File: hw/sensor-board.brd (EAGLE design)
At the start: 50 x 40 mm, 17 parts, among them U1 LT1762EMS8-3.3PBF, U2 ULN2003LVPWR, U3 ULN2003LVPWR, U4 PCA9685PW, U5 AT42QT1110-AU, X1 MOLEX-501331-1007, X2 MOLEX-501953-0407, X3 MOLEX-501953-0407, X4 MOLEX-501953-0407

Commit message: Update LED driver package for easier hand soldering.
New land patterns for PCA9685PW and ULN2003LV hae 0.5 mm of pads
extending past the IC pins to allow the soldering iron to make contact
with the pad.
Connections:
- new net VDD: U4.28
- net VDD_5: no longer U4.28
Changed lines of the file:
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@@
 </signal>
 <signal name="VDD_5">
-<contactref element="U4" pad="28"/>
 <contactref element="U1" pad="5"/>
 <contactref element="U1" pad="8"/>
@@
 </signal>
 <signal name="GND">
-<contactref element="U4" pad="14"/>
 <contactref element="U5" pad="5"/>
 <contactref element="U5" pad="21"/>
@@
 <contactref element="U2" pad="8"/>
 <contactref element="U3" pad="8"/>
+<contactref element="U4" pad="14"/>
 <wire x1="25.95" y1="33.1" x2="34.55" y2="33.9" width="0" layer="19" extent="1-1"/>
 <wire x1="16.3" y1="32.525" x2="25.95" y2="33.1" width="0" layer="19" extent="1-1"/>
 <wire x1="5.775" y1="11" x2="16.3" y2="32.525" width="0" layer="19" extent="1-1"/>
 <wire x1="5.775" y1="9" x2="5.775" y2="11" width="0" layer="19" extent="1-1"/>
-<wire x1="17.025" y1="2.45" x2="5.775" y2="9" width="0" layer="19" extent="1-1"/>
-<wire x1="22.6625" y1="1.775" x2="17.025" y2="2.45" width="0" layer="19" extent="1-1"/>
-<wire x1="37.775" y1="2.2" x2="22.6625" y2="1.775" width="0" layer="19" extent="1-1"/>
+<wire x1="17.025" y1="2.3" x2="5.775" y2="9" width="0" layer="19" extent="1-1"/>
+<wire x1="22.4625" y1="1.775" x2="17.025" y2="2.3" width="0" layer="19" extent="1-1"/>
+<wire x1="37.775" y1="2.05" x2="22.4625" y2="1.775" width="0" layer="19" extent="1-1"/>
 <wire x1="-5.875" y1="-14.75" x2="5.775" y2="9" width="0" layer="19" extent="1-1"/>
 <wire x1="-5.875" y1="-19" x2="-5.875" y2="-14.75" width="0" layer="19" extent="1-1"/>
@@
 <wire x1="5.775" y1="3" x2="31.45" y2="29.2" width="0" layer="19" extent="1-1"/>
 </signal>
+<signal name="VDD">
+<contactref element="U4" pad="28"/>
+</signal>
 </signals>

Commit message: Connect capsense controller/buttons/B2B connector.
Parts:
- added C10, C11, C12, C5, C6, C7, C8, C9: 0.015uF 16V, rcl:C0402K
- added R1, R2, R3, R4, R5, R6, R7, R8: 4.7k, myrcl:R0402
- added TP1, TP2, TP3, TP4: PTR1TP06R, testpad:TP06R
- C2, C3, C4: device rcl:C0603K -> rcl:C0402K
- moved X4 41.2 mm to (45.5, 31.2)
- moved X3 40.2 mm to (5.50, 31.2)
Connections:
- net N$6 renamed VDD_3_3
- new net N$10: C8.1, U5.8
- new net N$11: C9.1, U5.10
- new net N$12: C10.1, U5.12
- new net N$13: C11.1, U5.20
- new net N$14: C12.1, U5.23
- new net N$15: C5.2, R1.1, U5.1
- new net N$16: C6.2, R2.1, U5.3
- new net N$17: C7.2, R3.1, U5.6
- new net N$18: C8.2, R4.1, U5.9
- new net N$19: C9.2, R5.1, U5.11
- new net N$20: C10.2, R6.1, U5.13
- new net N$21: C11.2, R7.1, U5.19
- new net N$22: C12.2, R8.1, U5.22
- new net N$23: R5.2, X4.1
- new net N$24: R6.2, X4.2
- new net N$25: R7.2, X4.3
- new net N$26: R8.2, X4.4
- new net N$27: R4.2, TP4.TP, X3.4
- new net N$28: R3.2, TP3.TP, X3.3
- new net N$29: R2.2, TP2.TP, X3.2
- new net N$30: R1.2, TP1.TP, X3.1
- new net N$6: C5.1, U5.32
- new net N$7: C6.1, U5.2
- new net N$9: C7.1, U5.7

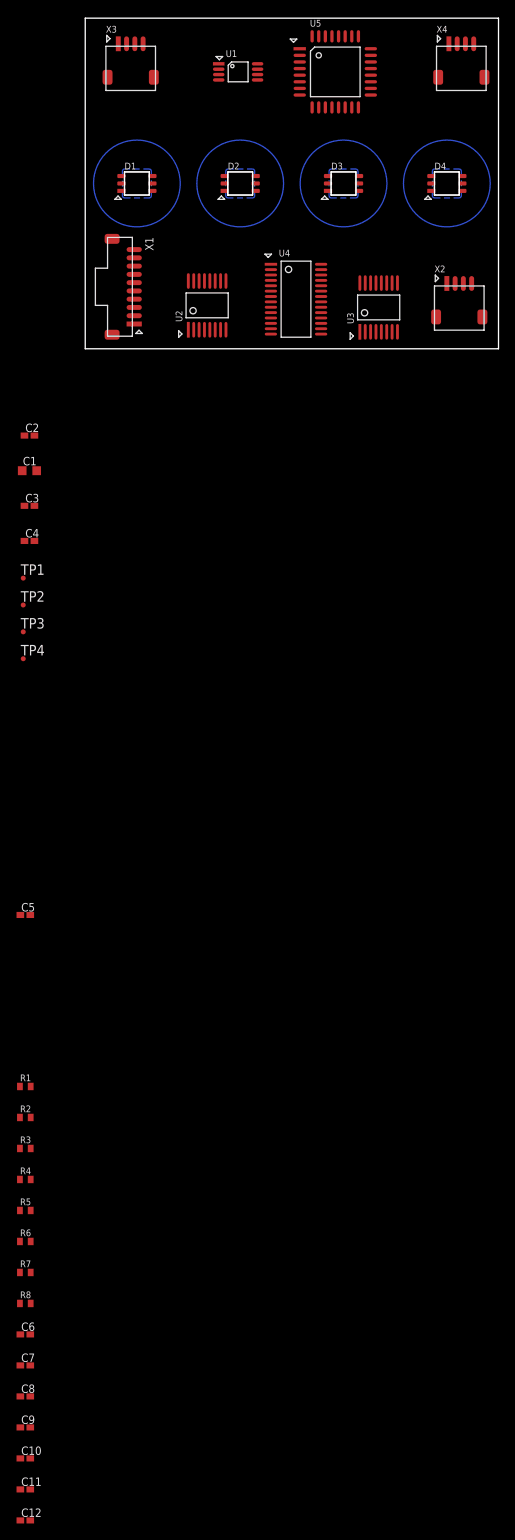
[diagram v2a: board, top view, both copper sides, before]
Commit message: Partly complete layout.
Pending schematic tasks:
1.  Replace 10 pin sensor board to main board connector with a higher
    pin count variant for unrouted signals on LED controller and
    RST,CHANGE pins on touch controller.
2.  Add pull ups on control and comm lines of touch and led ICs,
    as needed.
3.  Add mecahnism to set I2C address on LED controller.
4.  Identify purpose of and route COM pin on ULN2003LV.

Pending layout tasks:
1.  Route power and ground to top half and bottom right parts of board.
2.  Consider rotating touch IC 90 degrees counter clockwise to better
    match positions of b2b sensor connector and capsense buttons.
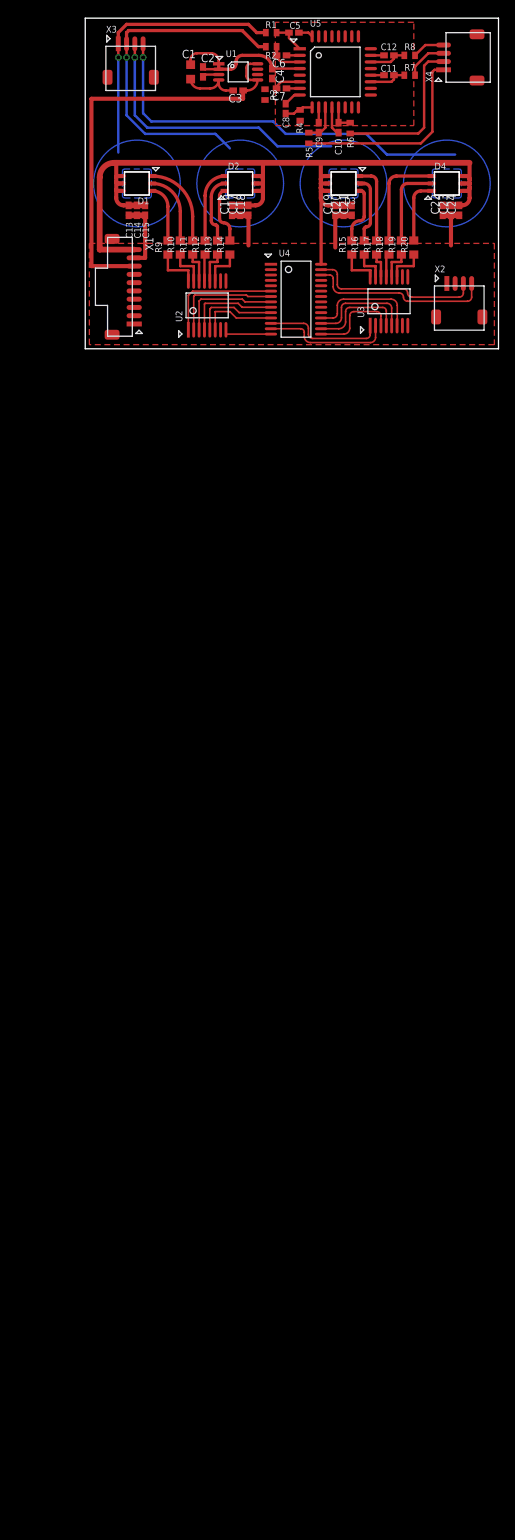
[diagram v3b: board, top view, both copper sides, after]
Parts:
- removed TP1, TP2, TP3, TP4: PTR1TP06R, testpad:TP06R
- added C13, C14, C15, C16, C17, C18, C19, C20, C21, C22, C23, C24: 0.01uF 16V, rcl:C0402K
- added R10, R11, R12, R13, R14, R15, R16, R17, R18, R19, R20, R9: 60R 145mW, myrcl:R0603
- moved C12 182.6 mm to (36.8, 35.5)
- moved C11 176.7 mm to (36.8, 33.1)
- moved C10 165.4 mm to (30.6, 26.8), turned to 90 degrees
- moved C9 161.2 mm to (28.2, 26.8), turned to 270 degrees
- moved C8 159.0 mm to (24.2, 29.1), turned to 270 degrees
- moved R8 158.0 mm to (39.2, 35.5)
- moved C6 157.8 mm to (23.8, 35.5), turned to 180 degrees
- moved C7 157.6 mm to (23.8, 31.5), turned to 180 degrees
- moved R7 152.1 mm to (39.2, 33.1)
- moved R6 140.3 mm to (32.0, 26.7), turned to 270 degrees
- moved R5 134.2 mm to (27.1, 25.5), turned to 270 degrees
- moved R4 133.0 mm to (26.0, 28.2), turned to 270 degrees
- moved R2 132.9 mm to (22.5, 36.5), turned to 180 degrees
- moved R1 130.9 mm to (22.5, 38.2), turned to 180 degrees
- moved R3 130.8 mm to (21.8, 30.8), turned to 270 degrees
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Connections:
- removed net N$27: R4.2, TP4.TP, X3.4
- removed net N$28: R3.2, TP3.TP, X3.3
- removed net N$29: R2.2, TP2.TP, X3.2
- removed net N$30: R1.2, TP1.TP, X3.1
- removed net VDD: U4.28
- new net KEY1: R1.2, X3.1
- new net KEY2: R2.2, X3.2
- new net KEY3: R3.2, X3.3
- new net KEY4: R4.2, X3.4
- new net LEDOUT_A1: U2.1, U4.6
- new net LEDOUT_A2: U2.2, U4.7
- new net LEDOUT_A3: U2.3, U4.8
- new net LEDOUT_A4: U2.4, U4.9
- new net LEDOUT_A5: U2.5, U4.10
- new net LEDOUT_A6: U2.6, U4.11
- new net LEDOUT_B1: U3.1, U4.12
- new net LEDOUT_B2: U3.2, U4.13
- new net LEDOUT_B3: U3.3, U4.15
- new net LEDOUT_B4: U3.4, U4.16
- new net LEDOUT_B5: U3.5, U4.17
- new net LEDOUT_B6: U3.6, U4.18
- new net N$31: D4.1, R20.2
- new net N$32: D1.1, R11.2
- new net N$33: D1.2, R10.2
- new net N$34: D3.3, R15.2
- new net N$35: D2.3, R12.2
- new net N$36: D2.2, R13.2
- new net N$37: R15.1, U3.16
- new net N$38: R16.1, U3.15
- new net N$39: D3.1, R17.2
- new net N$40: D3.2, R16.2
- new net N$41: D4.3, R18.2
- new net N$42: D4.2, R19.2
- new net N$55: R17.1, U3.14
- new net N$56: R18.1, U3.13
- new net N$57: R19.1, U3.12
- new net N$58: R20.1, U3.11
- new net N$59: D2.1, R14.2
- new net N$60: D1.3, R9.2
- new net N$61: R9.1, U2.16
- new net N$62: R10.1, U2.15
- new net N$63: R11.1, U2.14
- new net N$64: R12.1, U2.13
- new net N$65: R13.1, U2.12
- new net N$66: R14.1, U2.11
- new net SCL: U4.26, X2.4
- new net SDA: U4.27, X2.3
- net GND: now also C13.1, C14.1, C15.1, C16.1, C17.1, C18.1, C19.1, C20.1, C21.1, C22.1, C23.1, C24.1, X2.2
- net VDD_5: now also C13.2, C14.2, C15.2, C16.2, C17.2, C18.2, C19.2, C20.2, C21.2, C22.2, C23.2, C24.2, D1.4, D1.5, D1.6, D2.4, D2.5, D2.6, D3.4, D3.5, D3.6, D4.4, D4.5, D4.6, U4.28, X1.1, X2.1
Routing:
- net VDD_5: track 0.00 -> 162.6 mm
- net KEY4: track 0.00 -> 48.2 mm, vias 0 -> 1
- net KEY2: track 0.00 -> 41.9 mm, vias 0 -> 1
- net GND: track 0.00 -> 40.5 mm
- net KEY3: track 0.00 -> 34.0 mm, vias 0 -> 1
- net KEY1: track 0.00 -> 33.2 mm, vias 0 -> 1
- net N$23: track 0.00 -> 24.2 mm
- net SCL: track 0.00 -> 22.0 mm
- net SDA: track 0.00 -> 20.7 mm
- net VDD_3_3: track 0.00 -> 19.7 mm
- net N$24: track 0.00 -> 19.3 mm
- net LEDOUT_B2: track 0.00 -> 15.3 mm
- net LEDOUT_B1: track 0.00 -> 14.5 mm
- net LEDOUT_A1: track 0.00 -> 14.4 mm
- net LEDOUT_A2: track 0.00 -> 13.5 mm
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- added copper zone on layer 1, net GND
- added copper zone on layer 16, net KEY1
- added copper zone on layer 16, net KEY2
- added copper zone on layer 16, net KEY3
- added copper zone on layer 16, net KEY4
- removed copper zone on layer 16, net N$1

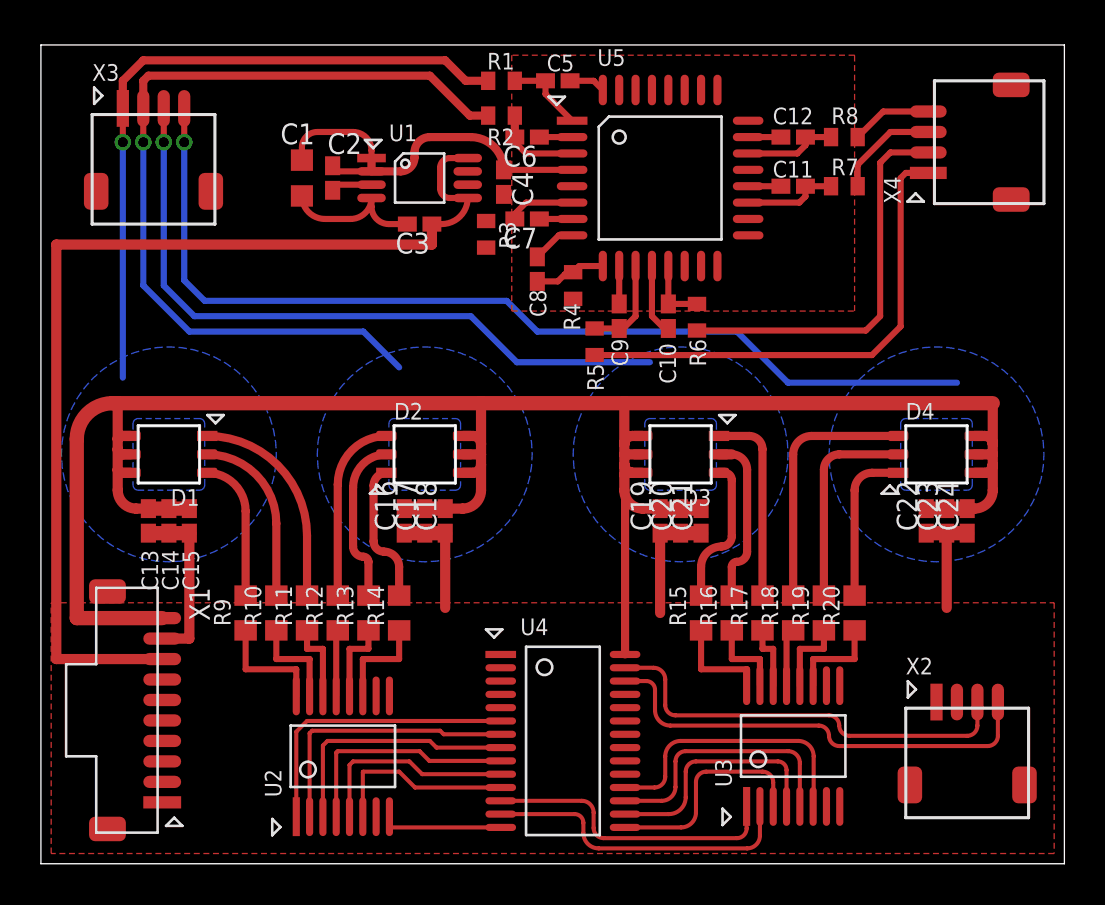
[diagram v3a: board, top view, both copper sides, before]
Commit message: Compact the layout of LED driving circuitry.
Additional space has been created for a larger sensor to main board
connector.
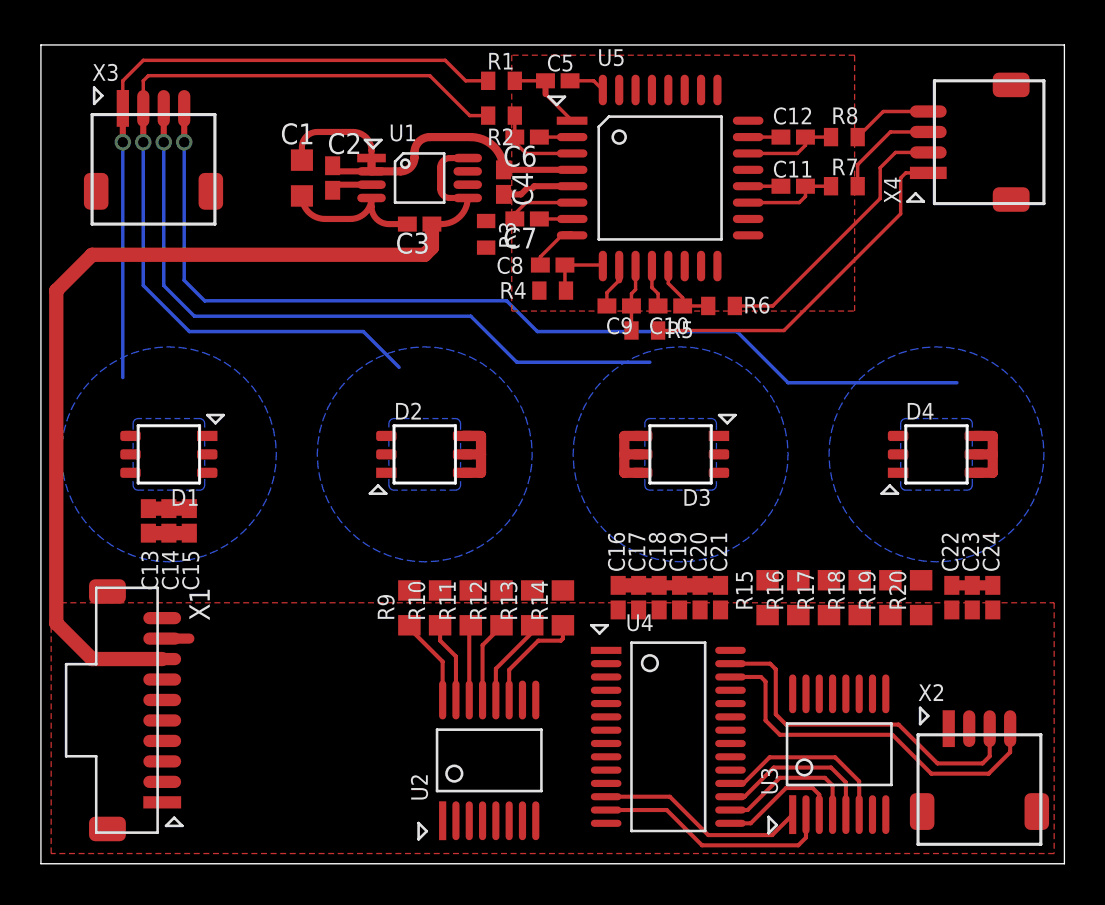
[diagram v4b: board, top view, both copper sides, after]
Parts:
- moved C16 11.1 mm to (28.2, 13.0)
- moved C17 11.1 mm to (29.2, 13.0)
- moved C18 11.1 mm to (30.2, 13.0)
- moved R10 8.00 mm to (19.5, 12.5)
- moved R11 8.00 mm to (21.0, 12.5)
- moved R12 8.00 mm to (22.5, 12.5)
- moved R13 8.00 mm to (24.0, 12.5)
- moved R14 8.00 mm to (25.5, 12.5)
- moved R9 8.00 mm to (18.0, 12.5)
- moved U2 7.15 mm to (21.9, 5.05)
- moved U4 5.15 mm to (30.6, 6.20)
- moved C22 3.95 mm to (44.5, 13.0)
- moved C23 3.95 mm to (45.5, 13.0)
- moved C24 3.95 mm to (46.5, 13.0)
- moved C20 3.87 mm to (32.2, 13.0)
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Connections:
- net GND: now also U4.24, U4.25, U4.3, U4.4, U4.5
- net VDD_5: now also U2.9, U3.9
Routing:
- net VDD_5: track 162.6 -> 72.2 mm
- net GND: track 40.5 -> 13.4 mm
- net LEDOUT_A1: track 14.4 -> 0.00 mm
- net LEDOUT_A2: track 13.5 -> 0.00 mm
- net N$41: track 12.4 -> 0.00 mm
- net LEDOUT_A3: track 12.4 -> 0.00 mm
- net LEDOUT_A4: track 11.4 -> 0.00 mm
- net LEDOUT_A5: track 10.2 -> 0.00 mm
- net N$42: track 10.1 -> 0.00 mm
- net N$32: track 9.82 -> 0.00 mm
- net N$39: track 9.54 -> 0.00 mm
- net LEDOUT_A6: track 9.24 -> 0.00 mm
- net N$35: track 8.78 -> 0.00 mm
- net N$33: track 8.30 -> 0.00 mm
- net N$40: track 8.15 -> 0.00 mm
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
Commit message: Change capsense IC to QT1070. Routing finished.
Schematic and routing need to be checked against LED and CAPSENSE IC
datasheets wrt operational requirements.
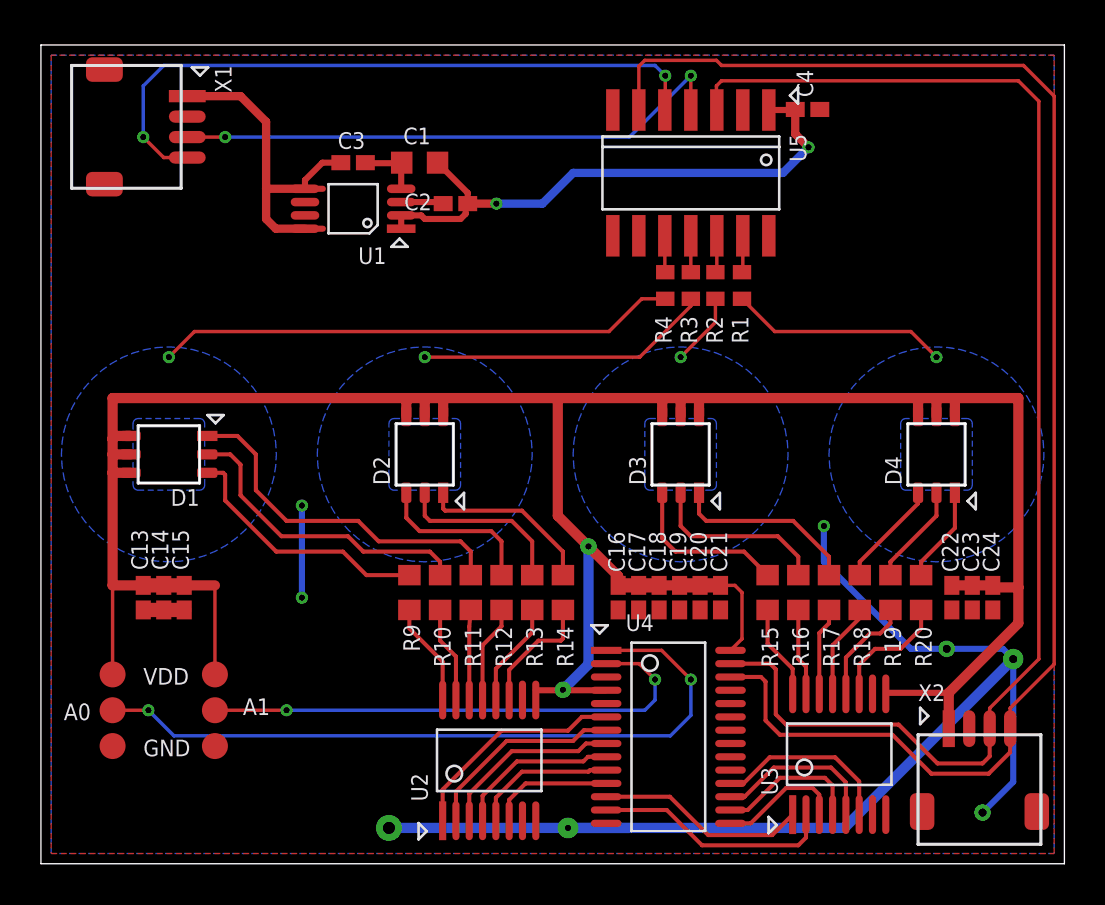
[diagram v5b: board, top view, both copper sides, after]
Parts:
- removed C10, C11, C12, C5, C6, C7, C8, C9: 0.015uF 16V, rcl:C0402K
- removed R5, R6, R7, R8: 4.7k, myrcl:R0402
- removed X3, X4: MOLEX-501953-0407, connector:MOLEX-501953-0407
- added A0, A1, GND, TP1, TP3, VDD: TPB1,27, testpad:B1,27
- U5: value AT42QT1110-AU -> AT42QT1070-SSU; device touch_ctl:AT42QT1110-AU -> touch_ctl:SO14
- X1: value MOLEX-501331-1007 -> MOLEX-501953-0407; device connector:MOLEX-501331-1007 -> connector:MOLEX-501953-0407
- moved X1 28.6 mm to (1.50, 36.0)
- moved R1 15.4 mm to (34.2, 28.2), turned to 270 degrees
- moved C4 15.3 mm to (37.5, 36.9), turned to 0 degrees
- moved R2 13.3 mm to (33.0, 28.2), turned to 270 degrees
- moved R3 10.3 mm to (31.8, 28.2)
- moved C2 6.13 mm to (20.2, 32.2), turned to 0 degrees
- moved C1 5.80 mm to (18.5, 34.2), turned to 180 degrees
- moved R4 5.51 mm to (30.5, 28.2), turned to 270 degrees
- moved C3 4.42 mm to (15.2, 34.2), turned to 0 degrees
- moved C13 3.76 mm to (5.00, 13.0)
- moved C14 3.76 mm to (6.00, 13.0)
- moved C15 3.76 mm to (7.00, 13.0)
- moved U1 3.58 mm to (15.2, 32.0), turned to 180 degrees
- moved U5 1.52 mm to (31.8, 33.8), turned to 180 degrees
- moved R10 0.75 mm to (19.5, 13.2)
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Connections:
- removed net CAPSENSE1: U5.29, X1.5
- removed net CAPSENSE2: U5.28, X1.6
- removed net CAPSENSE3: U5.15, X1.7
- removed net CAPSENSE4: U5.16, X1.8
- removed net CAPSENSE5: U5.17, X1.9
- removed net CAPSENSE6: U5.14, X1.10
- removed net N$10: C8.1, U5.8
- removed net N$11: C9.1, U5.10
- removed net N$12: C10.1, U5.12
- removed net N$13: C11.1, U5.20
- removed net N$14: C12.1, U5.23
- removed net N$19: C9.2, R5.1, U5.11
- removed net N$20: C10.2, R6.1, U5.13
- removed net N$21: C11.2, R7.1, U5.19
- removed net N$22: C12.2, R8.1, U5.22
- removed net N$23: R5.2, X4.1
- removed net N$24: R6.2, X4.2
- removed net N$25: R7.2, X4.3
- removed net N$26: R8.2, X4.4
- removed net N$9: C7.1, U5.7
- new net !CAPSENSE_CHG!: U5.5, X1.4
- new net !CAPSENSE_RST!: U5.4, X1.3
- net GND: now also GND.TP, TP3.TP, U4.23, U5.14, U5.2; no longer U4.4, U5.21, U5.5, X1.4
- net KEY1: no longer X3.1
- net KEY2: no longer X3.2
- net KEY3: no longer X3.3
- net KEY4: no longer X3.4
- net N$15: now also U5.13; no longer C5.2, U5.1
- net N$16: now also U5.12; no longer C6.2, U5.3
- net N$17: now also U5.11; no longer C7.2, U5.6
- net N$18: now also U5.10; no longer C8.2, U5.9
- net N$6: now also A0.TP, U4.1; no longer C5.1, U5.32
- net N$7: now also A1.TP, U4.2; no longer C6.1, U5.2
- net N$8: now also C2.1; no longer C2.2
- net SCL: now also U5.6
- net SDA: now also U5.3
- net VDD_3_3: now also C2.2, U5.1; no longer C2.1, U5.18, U5.4
- net VDD_5: now also TP1.TP, U4.4, VDD.TP; no longer X1.3
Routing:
- net VDD_5: track 72.2 -> 150.7 mm, vias 0 -> 2
- net SCL: track 18.3 -> 73.4 mm
- net GND: track 13.4 -> 67.6 mm, vias 0 -> 8
- net SDA: track 17.5 -> 66.6 mm
- net KEY2: track 41.9 -> 3.55 mm
- net N$6: track 1.79 -> 35.7 mm, vias 0 -> 2
- net !CAPSENSE_CHG!: track 0.00 -> 32.9 mm, vias 0 -> 2
- net !CAPSENSE_RST!: track 0.00 -> 27.5 mm, vias 0 -> 2
- net N$7: track 1.60 -> 25.4 mm, vias 0 -> 2
- net KEY4: track 48.2 -> 25.4 mm
- net KEY1: track 33.2 -> 10.7 mm
- net KEY3: track 34.0 -> 14.4 mm
- net N$23: track 17.4 -> 0.00 mm
- net N$32: track 0.00 -> 17.4 mm
- net N$33: track 0.00 -> 15.1 mm
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- added copper zone on layer 16, net GND
